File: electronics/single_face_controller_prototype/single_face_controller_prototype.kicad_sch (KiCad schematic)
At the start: 1 part

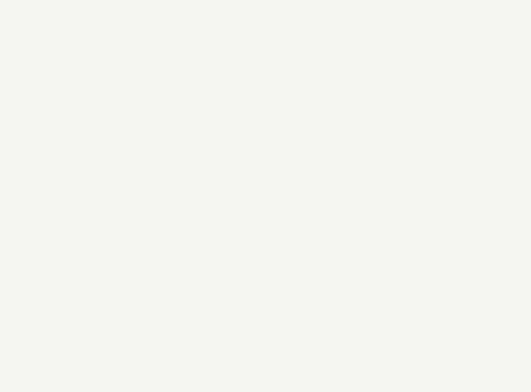
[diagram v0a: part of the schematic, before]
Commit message: Add CSD17575Q3 30V 27A MOSFET to library
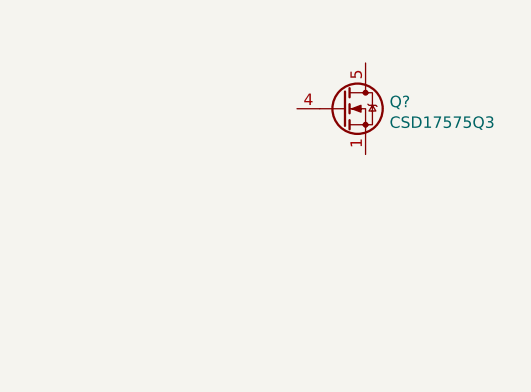
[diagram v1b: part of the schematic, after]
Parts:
- added Q?: CSD17575Q3, Package_SON:VSON-8_3.3x3.3mm_P0.65mm_NexFET, symbol User:CSD17575Q3
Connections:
- new net: Q?.1 (S), Q?.2 (S), Q?.3 (S)
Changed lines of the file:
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@@
 (kicad_sch (version 20210126) (generator eeschema)
   (paper "A4")
+  (symbol (lib_id "User:CSD17575Q3") (at 195.58 68.58 0) (unit 1)
+    (in_bom yes) (on_board yes)
+    (property "Reference" "Q?" (id 0) (at 200.7871 67.8191 0)
+      (effects (font (size 1.27 1.27)) (justify left))
+    )
+    (property "Value" "CSD17575Q3" (id 1) (at 200.7871 70.1178 0)
+      (effects (font (size 1.27 1.27)) (justify left))
+    )
+    (property "Footprint" "Package_SON:VSON-8_3.3x3.3mm_P0.65mm_NexFET" (id 2) (at 200.66 70.485 0)
+      (effects (font (size 1.27 1.27) italic) (justify left) hide)
+    )
+    (property "Datasheet" "https://www.ti.com/lit/gpn/csd17575q3" (id 3) (at 195.58 68.58 90)
+      (effects (font (size 1.27 1.27)) (justify left) hide)
+    )
+    (pin "1")
+    (pin "2")
+    (pin "3")
+    (pin "4")
+    (pin "5")
+  )
   (symbol (lib_id "User:STSPIN32F0A") (at 127 101.6 0) (unit 1)
     (in_bom yes) (on_board yes)
@@
   )
   (symbol_instances
+    (path "/c3280120-51c4-4791-922f-7c9c409ee9a9"
+      (reference "Q?") (unit 1) (value "CSD17575Q3") (footprint "Package_SON:VSON-8_3.3x3.3mm_P0.65mm_NexFET")
+    )
     (path "/6b0556ca-7022-41ff-af7b-e2a327ac1698"
       (reference "U?") (unit 1) (value "STSPIN32F0A") (footprint "")

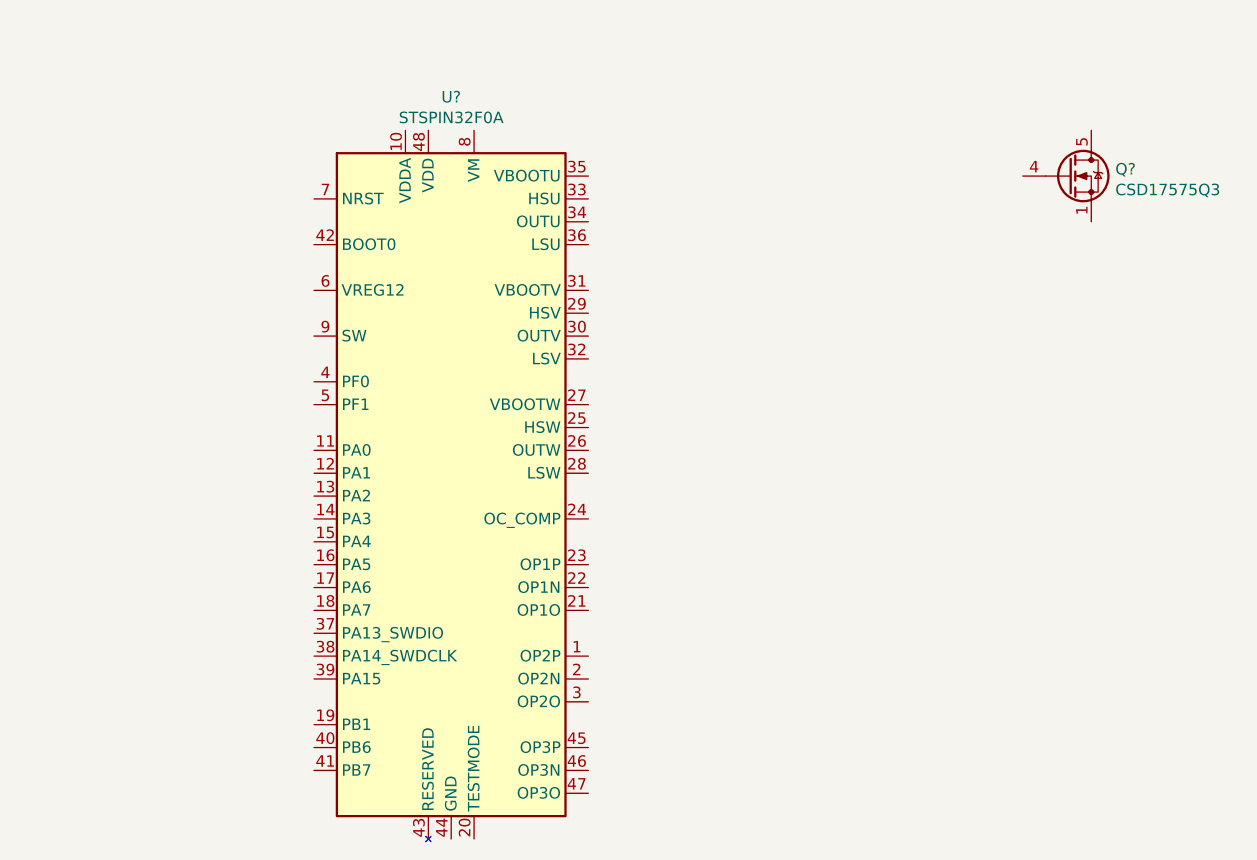
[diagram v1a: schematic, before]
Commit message: Add switching inductor+diode
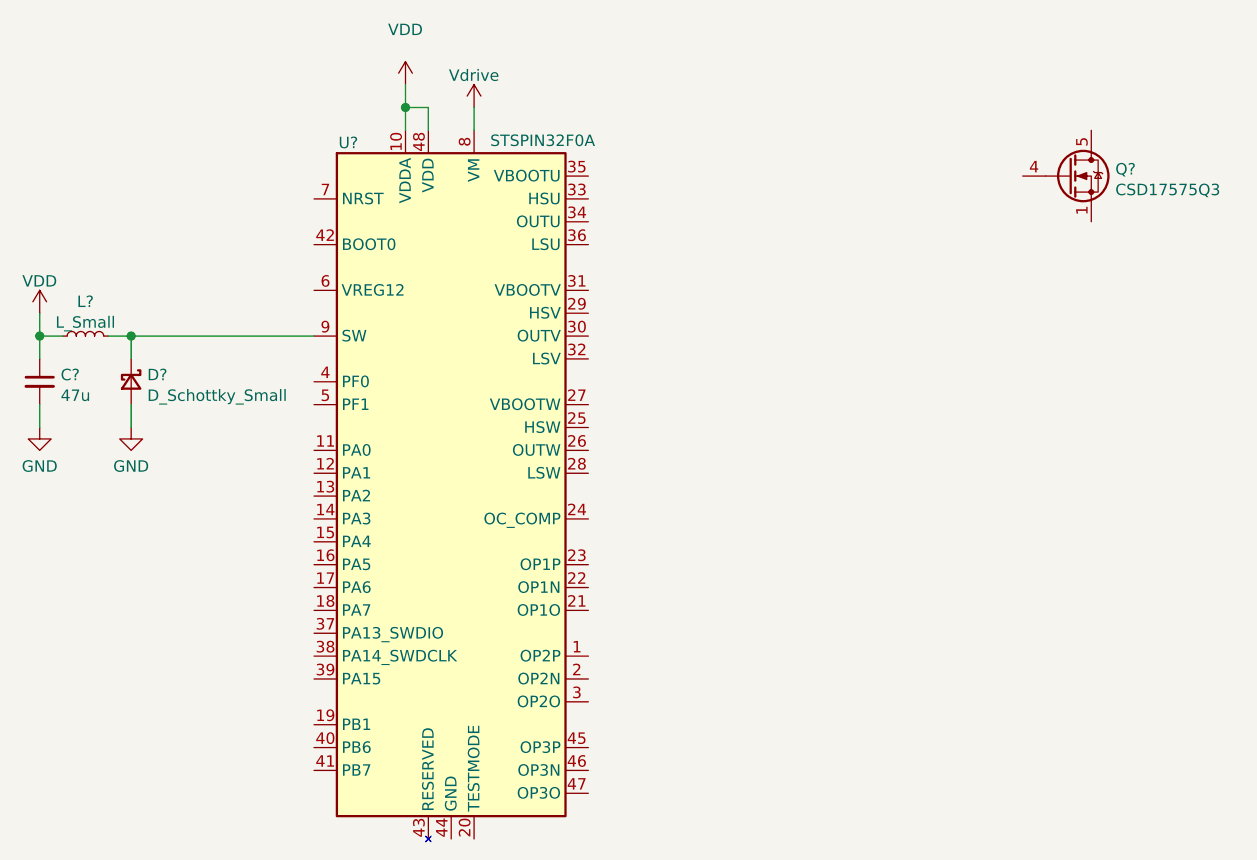
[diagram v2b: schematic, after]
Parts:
- added C?: 47u, symbol Device:C_Small
- added D?: D_Schottky_Small, symbol Device:D_Schottky_Small
- added L?: L_Small, symbol Device:L_Small
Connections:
- net VDD: now reaches U?.10 (VDDA)
- net VDD: now also U?.48 (VDD), C?.1, L?.1
- net Vdrive: now reaches U?.8 (VM)
- net at U?.9 (SW): now also D?.1 (K), L?.2
- new net GND: C?.2, D?.2 (A)
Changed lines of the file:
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@@
 (kicad_sch (version 20210126) (generator eeschema)
   (paper "A4")
+  (junction (at 81.28 86.36) (diameter 1.016) (color 0 0 0 0))
+  (junction (at 91.44 86.36) (diameter 1.016) (color 0 0 0 0))
+  (junction (at 121.92 60.96) (diameter 1.016) (color 0 0 0 0))
+  (wire (pts (xy 81.28 83.82) (xy 81.28 86.36))
+    (stroke (width 0) (type solid) (color 0 0 0 0))
+  )
+  (wire (pts (xy 81.28 86.36) (xy 81.28 88.9))
+    (stroke (width 0) (type solid) (color 0 0 0 0))
+  )
+  (wire (pts (xy 81.28 86.36) (xy 83.82 86.36))
+    (stroke (width 0) (type solid) (color 0 0 0 0))
+  )
+  (wire (pts (xy 81.28 93.98) (xy 81.28 96.52))
+    (stroke (width 0) (type solid) (color 0 0 0 0))
+  )
+  (wire (pts (xy 88.9 86.36) (xy 91.44 86.36))
+    (stroke (width 0) (type solid) (color 0 0 0 0))
+  )
+  (wire (pts (xy 91.44 86.36) (xy 91.44 88.9))
+    (stroke (width 0) (type solid) (color 0 0 0 0))
+  )
+  (wire (pts (xy 91.44 86.36) (xy 111.76 86.36))
+    (stroke (width 0) (type solid) (color 0 0 0 0))
+  )
+  (wire (pts (xy 91.44 93.98) (xy 91.44 96.52))
+    (stroke (width 0) (type solid) (color 0 0 0 0))
+  )
+  (wire (pts (xy 121.92 58.42) (xy 121.92 60.96))
+    (stroke (width 0) (type solid) (color 0 0 0 0))
+  )
+  (wire (pts (xy 121.92 60.96) (xy 121.92 63.5))
+    (stroke (width 0) (type solid) (color 0 0 0 0))
+  )
+  (wire (pts (xy 121.92 60.96) (xy 124.46 60.96))
+    (stroke (width 0) (type solid) (color 0 0 0 0))
+  )
+  (wire (pts (xy 124.46 60.96) (xy 124.46 63.5))
+    (stroke (width 0) (type solid) (color 0 0 0 0))
+  )
+  (wire (pts (xy 129.54 60.96) (xy 129.54 63.5))
+    (stroke (width 0) (type solid) (color 0 0 0 0))
+  )
+  (symbol (lib_id "power:VDD") (at 81.28 83.82 0) (unit 1)
+    (in_bom yes) (on_board yes)
+    (property "Reference" "#PWR?" (id 0) (at 81.28 87.63 0)
+      (effects (font (size 1.27 1.27)) hide)
+    )
+    (property "Value" "VDD" (id 1) (at 81.28 80.2726 0))
+    (property "Footprint" "" (id 2) (at 81.28 83.82 0)
+      (effects (font (size 1.27 1.27)) hide)
+    )
+    (property "Datasheet" "" (id 3) (at 81.28 83.82 0)
+      (effects (font (size 1.27 1.27)) hide)
+    )
+    (pin "1")
+  )
+  (symbol (lib_id "power:VDD") (at 121.92 58.42 0) (unit 1)
+    (in_bom yes) (on_board yes)
+    (property "Reference" "#PWR?" (id 0) (at 121.92 62.23 0)
+      (effects (font (size 1.27 1.27)) hide)
+    )
+    (property "Value" "VDD" (id 1) (at 121.92 52.3326 0))
+    (property "Footprint" "" (id 2) (at 121.92 58.42 0)
+      (effects (font (size 1.27 1.27)) hide)
+    )
+    (property "Datasheet" "" (id 3) (at 121.92 58.42 0)
+      (effects (font (size 1.27 1.27)) hide)
+    )
+    (pin "1")
+  )
+  (symbol (lib_id "power:Vdrive") (at 129.54 60.96 0) (unit 1)
+    (in_bom yes) (on_board yes)
+    (property "Reference" "#PWR?" (id 0) (at 124.46 64.77 0)
+      (effects (font (size 1.27 1.27)) hide)
+    )
+    (property "Value" "Vdrive" (id 1) (at 129.54 57.4126 0))
+    (property "Footprint" "" (id 2) (at 129.54 60.96 0)
+      (effects (font (size 1.27 1.27)) hide)
+    )
+    (property "Datasheet" "" (id 3) (at 129.54 60.96 0)
+      (effects (font (size 1.27 1.27)) hide)
+    )
+    (pin "1")
+  )
+  (symbol (lib_id "Device:L_Small") (at 86.36 86.36 90) (unit 1)
+    (in_bom yes) (on_board yes)
+    (property "Reference" "L?" (id 0) (at 86.36 82.5458 90))
+    (property "Value" "L_Small" (id 1) (at 86.36 84.8445 90))
+    (property "Footprint" "" (id 2) (at 86.36 86.36 0)
+      (effects (font (size 1.27 1.27)) hide)
+    )
+    (property "Datasheet" "~" (id 3) (at 86.36 86.36 0)
+      (effects (font (size 1.27 1.27)) hide)
+    )
+    (pin "1")
+    (pin "2")
+  )
+  (symbol (lib_id "power:GND") (at 81.28 96.52 0) (unit 1)
+    (in_bom yes) (on_board yes)
+    (property "Reference" "#PWR?" (id 0) (at 81.28 102.87 0)
+      (effects (font (size 1.27 1.27)) hide)
+    )
+    (property "Value" "GND" (id 1) (at 81.28 100.8444 0))
+    (property "Footprint" "" (id 2) (at 81.28 96.52 0)
+      (effects (font (size 1.27 1.27)) hide)
+    )
+    (property "Datasheet" "" (id 3) (at 81.28 96.52 0)
+      (effects (font (size 1.27 1.27)) hide)
+    )
+    (pin "1")
+  )
+  (symbol (lib_id "power:GND") (at 91.44 96.52 0) (unit 1)
+    (in_bom yes) (on_board yes)
+    (property "Reference" "#PWR?" (id 0) (at 91.44 102.87 0)
+      (effects (font (size 1.27 1.27)) hide)
+    )
+    (property "Value" "GND" (id 1) (at 91.44 100.8444 0))
+    (property "Footprint" "" (id 2) (at 91.44 96.52 0)
+      (effects (font (size 1.27 1.27)) hide)
+    )
+    (property "Datasheet" "" (id 3) (at 91.44 96.52 0)
+      (effects (font (size 1.27 1.27)) hide)
+    )
+    (pin "1")
+  )
+  (symbol (lib_id "Device:D_Schottky_Small") (at 91.44 91.44 270) (unit 1)
+    (in_bom yes) (on_board yes)
+    (property "Reference" "D?" (id 0) (at 93.2181 90.6791 90)
+      (effects (font (size 1.27 1.27)) (justify left))
+    )
+    (property "Value" "D_Schottky_Small" (id 1) (at 93.2181 92.9778 90)
+      (effects (font (size 1.27 1.27)) (justify left))
+    )
+    (property "Footprint" "" (id 2) (at 91.44 91.44 90)
+      (effects (font (size 1.27 1.27)) hide)
+    )
+    (property "Datasheet" "~" (id 3) (at 91.44 91.44 90)
+      (effects (font (size 1.27 1.27)) hide)
+    )
+    (pin "1")
+    (pin "2")
+  )
+  (symbol (lib_id "Device:C_Small") (at 81.28 91.44 0) (unit 1)
+    (in_bom yes) (on_board yes)
+    (property "Reference" "C?" (id 0) (at 83.6042 90.6791 0)
+      (effects (font (size 1.27 1.27)) (justify left))
+    )
+    (property "Value" "47u" (id 1) (at 83.6042 92.9778 0)
+      (effects (font (size 1.27 1.27)) (justify left))
+    )
+    (property "Footprint" "" (id 2) (at 81.28 91.44 0)
+      (effects (font (size 1.27 1.27)) hide)
+    )
+    (property "Datasheet" "~" (id 3) (at 81.28 91.44 0)
+      (effects (font (size 1.27 1.27)) hide)
+    )
+    (pin "1")
+    (pin "2")
+  )
   (symbol (lib_id "User:CSD17575Q3") (at 195.58 68.58 0) (unit 1)
     (in_bom yes) (on_board yes)
@@
   (symbol (lib_id "User:STSPIN32F0A") (at 127 101.6 0) (unit 1)
     (in_bom yes) (on_board yes)
-    (property "Reference" "U?" (id 0) (at 127 59.8128 0))
-    (property "Value" "STSPIN32F0A" (id 1) (at 127 62.1115 0))
+    (property "Reference" "U?" (id 0) (at 115.57 64.8928 0))
+    (property "Value" "STSPIN32F0A" (id 1) (at 137.16 64.6515 0))
     (property "Footprint" "" (id 2) (at 111.76 139.7 0)
       (effects (font (size 1.27 1.27)) (justify right) hide)
@@
   )
   (symbol_instances
+    (path "/9371b183-8bc1-4272-be3c-a46778be969e"
+      (reference "#PWR?") (unit 1) (value "GND") (footprint "")
+    )
+    (path "/9911f6be-1e03-47f5-b17f-89a74fd097c1"
+      (reference "#PWR?") (unit 1) (value "GND") (footprint "")
+    )
+    (path "/a96d66bb-df0f-4db6-99d4-b0cf880a68de"
+      (reference "#PWR?") (unit 1) (value "VDD") (footprint "")
+    )
+    (path "/cd4f5535-149b-46b3-92e6-92a9933a9f62"
+      (reference "#PWR?") (unit 1) (value "VDD") (footprint "")
+    )
+    (path "/e5d886a4-3c46-4c76-8d1d-f81a95e738c6"
+      (reference "#PWR?") (unit 1) (value "Vdrive") (footprint "")
+    )
+    (path "/ec439ee0-f658-4787-9aff-df44ad970900"
+      (reference "C?") (unit 1) (value "47u") (footprint "")
+    )
+    (path "/d793cdbe-b9f5-4044-9d4e-65b04e6eb6ff"
+      (reference "D?") (unit 1) (value "D_Schottky_Small") (footprint "")
+    )
+    (path "/4c1d5cb0-8e66-4b75-8824-25bdc58a2283"
+      (reference "L?") (unit 1) (value "L_Small") (footprint "")
+    )
     (path "/c3280120-51c4-4791-922f-7c9c409ee9a9"
       (reference "Q?") (unit 1) (value "CSD17575Q3") (footprint "Package_SON:VSON-8_3.3x3.3mm_P0.65mm_NexFET")
